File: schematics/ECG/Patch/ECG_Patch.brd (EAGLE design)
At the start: 11.6 x 27.7 mm, 10 parts

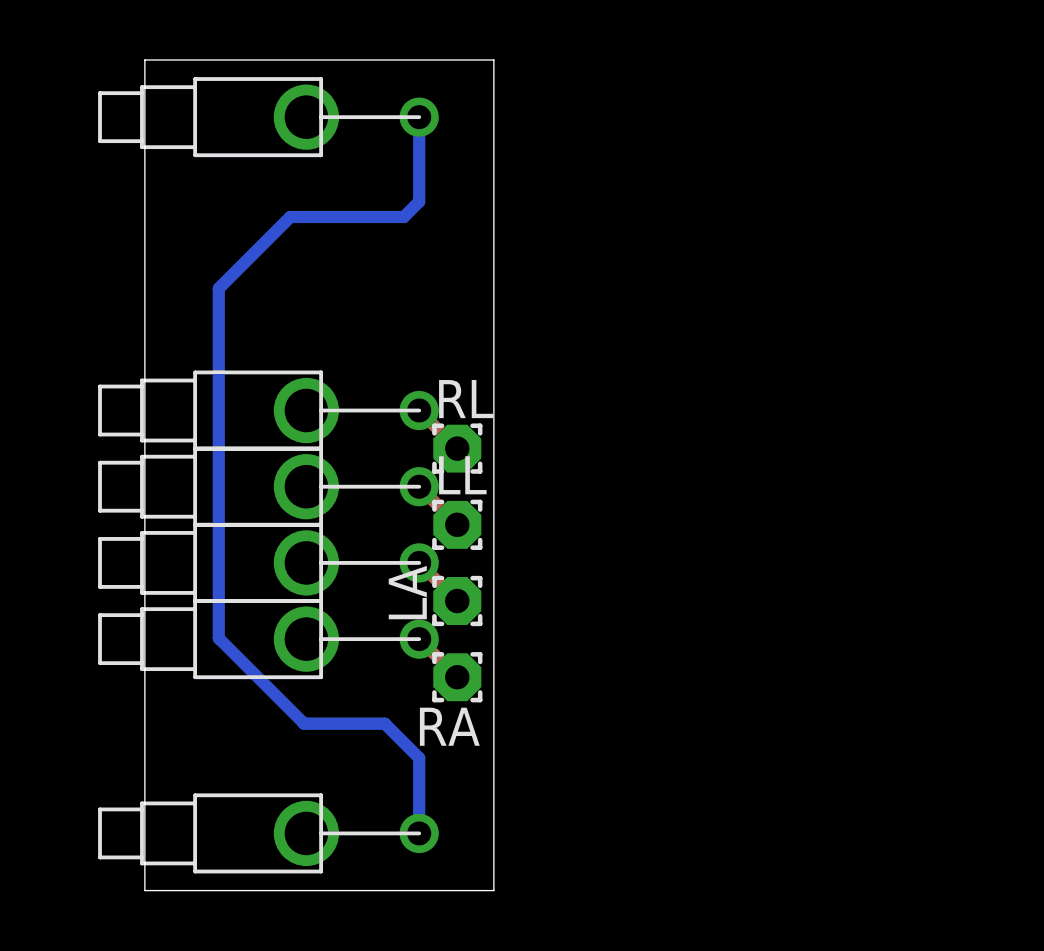
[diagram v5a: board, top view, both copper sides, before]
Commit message: tweaked traces
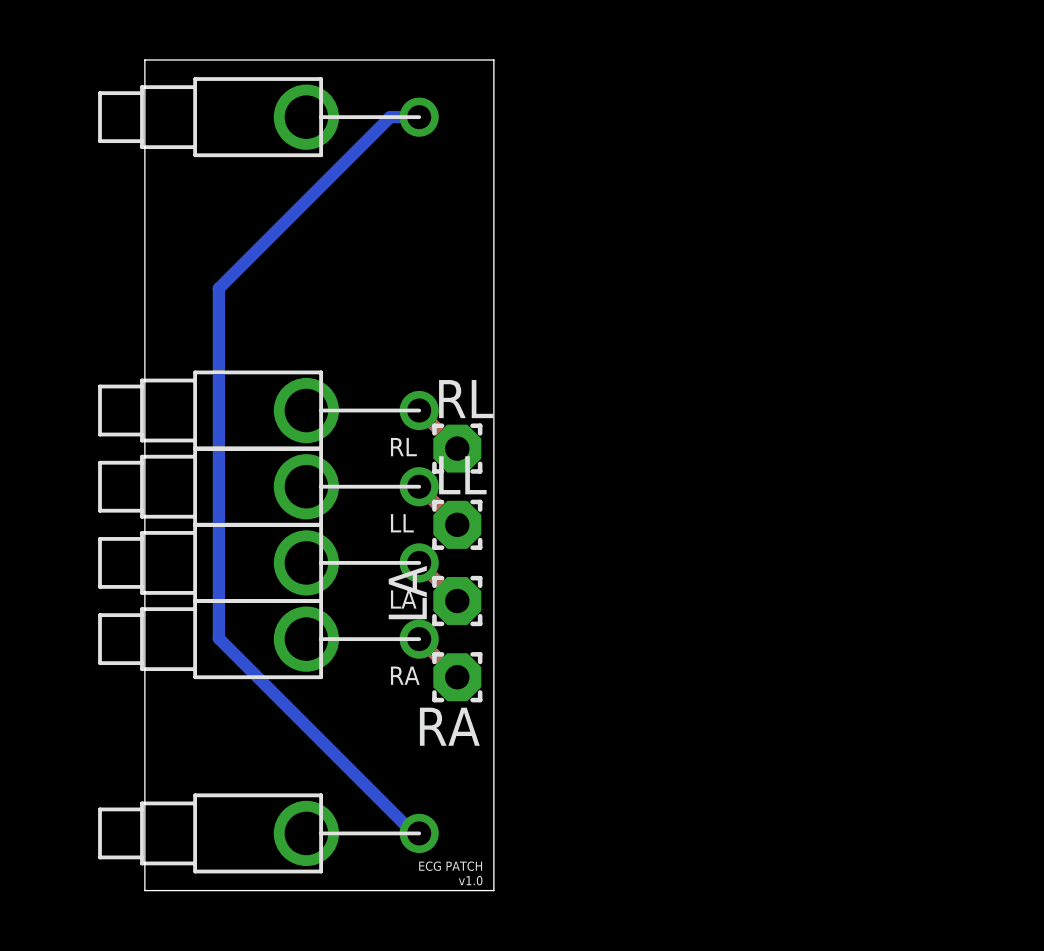
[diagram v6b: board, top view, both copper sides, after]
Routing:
- net BATT: track 33.2 -> 30.1 mm
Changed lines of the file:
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@@
 <wire x1="11.6332" y1="27.686" x2="0" y2="27.686" width="0" layer="20"/>
 <wire x1="0" y1="27.686" x2="0" y2="0" width="0" layer="20"/>
-<text x="8.128" y="14.478" size="0.6096" layer="48">RL</text>
-<text x="8.128" y="11.938" size="0.6096" layer="48">LL</text>
-<text x="8.128" y="9.398" size="0.6096" layer="48">LA</text>
-<text x="8.128" y="6.858" size="0.6096" layer="48">RA</text>
-<text x="11.2776" y="0.9652" size="0.3048" layer="48" rot="R180">ECG PATCH</text>
-<text x="11.2776" y="0.4826" size="0.3048" layer="48" rot="R180">v1.0</text>
+<text x="8.128" y="14.478" size="0.6096" layer="21">RL</text>
+<text x="8.128" y="11.938" size="0.6096" layer="21">LL</text>
+<text x="8.128" y="9.398" size="0.6096" layer="21">LA</text>
+<text x="8.128" y="6.858" size="0.6096" layer="21">RA</text>
+<text x="11.2776" y="0.9652" size="0.3048" layer="21" rot="R180">ECG PATCH</text>
+<text x="11.2776" y="0.4826" size="0.3048" layer="21" rot="R180">v1.0</text>
 </plain>
 <attributes>
@@
 <contactref element="U$6" pad="1"/>
 <wire x1="2.4638" y1="20.066" x2="2.4638" y2="8.4074" width="0.4064" layer="16"/>
-<wire x1="2.4638" y1="8.4074" x2="5.3086" y2="5.5626" width="0.4064" layer="16"/>
-<wire x1="9.144" y1="1.905" x2="9.144" y2="4.4196" width="0.4064" layer="16"/>
-<wire x1="9.144" y1="4.4196" x2="8.001" y2="5.5626" width="0.4064" layer="16"/>
-<wire x1="8.001" y1="5.5626" x2="5.3086" y2="5.5626" width="0.4064" layer="16"/>
-<wire x1="9.144" y1="25.781" x2="9.144" y2="22.9616" width="0.4064" layer="16"/>
-<wire x1="9.144" y1="22.9616" x2="8.636" y2="22.4536" width="0.4064" layer="16"/>
-<wire x1="8.636" y1="22.4536" x2="4.8514" y2="22.4536" width="0.4064" layer="16"/>
-<wire x1="4.8514" y1="22.4536" x2="2.4638" y2="20.066" width="0.4064" layer="16"/>
+<wire x1="9.144" y1="1.905" x2="8.9662" y2="1.905" width="0.4064" layer="16"/>
+<wire x1="8.9662" y1="1.905" x2="2.4638" y2="8.4074" width="0.4064" layer="16"/>
+<wire x1="9.144" y1="25.781" x2="8.1788" y2="25.781" width="0.4064" layer="16"/>
+<wire x1="8.1788" y1="25.781" x2="2.4638" y2="20.066" width="0.4064" layer="16"/>
 </signal>
 </signals>

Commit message: using updated millmax piston package with proper center origin
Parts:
- moved U$1 5.33 mm to (3.81, 16.0)
- moved U$2 5.33 mm to (3.81, 13.5)
- moved U$3 5.33 mm to (3.81, 10.9)
- moved U$4 5.33 mm to (3.81, 8.38)
- moved U$5 5.33 mm to (3.81, 25.8)
- moved U$6 5.33 mm to (3.81, 1.91)
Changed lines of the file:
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@@
 <?xml version="1.0" encoding="utf-8"?>
 <!DOCTYPE eagle SYSTEM "eagle.dtd">
-<eagle version="6.4">
+<eagle version="6.5.0">
 <drawing>
 <settings>
@@
 <layer number="220" name="220bmp" color="21" fill="1" visible="no" active="no"/>
 <layer number="221" name="221bmp" color="22" fill="1" visible="no" active="no"/>
-<layer number="222" name="222bmp" color="23" fill="1" visible="no" active="no"/>
 <layer number="223" name="223bmp" color="24" fill="1" visible="no" active="no"/>
 <layer number="224" name="224bmp" color="25" fill="1" visible="no" active="no"/>
@@
 </autorouter>
 <elements>
-<element name="U$1" library="pins" package="PISTON_RA_TH" value="PISTON_RA_TH" x="9.144" y="16.002" rot="R180"/>
-<element name="U$2" library="pins" package="PISTON_RA_TH" value="PISTON_RA_TH" x="9.144" y="13.462" rot="R180"/>
-<element name="U$3" library="pins" package="PISTON_RA_TH" value="PISTON_RA_TH" x="9.144" y="10.922" rot="R180"/>
-<element name="U$4" library="pins" package="PISTON_RA_TH" value="PISTON_RA_TH" x="9.144" y="8.382" rot="R180"/>
-<element name="U$5" library="pins" package="PISTON_RA_TH" value="PISTON_RA_TH" x="9.144" y="25.781" rot="R180"/>
-<element name="U$6" library="pins" package="PISTON_RA_TH" value="PISTON_RA_TH" x="9.144" y="1.905" rot="R180"/>
+<element name="U$1" library="pins" package="PISTON_RA_TH" value="PISTON_RA_TH" x="3.81" y="16.002" rot="R180"/>
+<element name="U$2" library="pins" package="PISTON_RA_TH" value="PISTON_RA_TH" x="3.81" y="13.462" rot="R180"/>
+<element name="U$3" library="pins" package="PISTON_RA_TH" value="PISTON_RA_TH" x="3.81" y="10.922" rot="R180"/>
+<element name="U$4" library="pins" package="PISTON_RA_TH" value="PISTON_RA_TH" x="3.81" y="8.382" rot="R180"/>
+<element name="U$5" library="pins" package="PISTON_RA_TH" value="PISTON_RA_TH" x="3.81" y="25.781" rot="R180"/>
+<element name="U$6" library="pins" package="PISTON_RA_TH" value="PISTON_RA_TH" x="3.81" y="1.905" rot="R180"/>
 <element name="LL" library="wirepad" package="1,6/0,8" value="" x="10.414" y="12.192"/>
 <element name="RL" library="wirepad" package="1,6/0,8" value="" x="10.414" y="14.732"/>

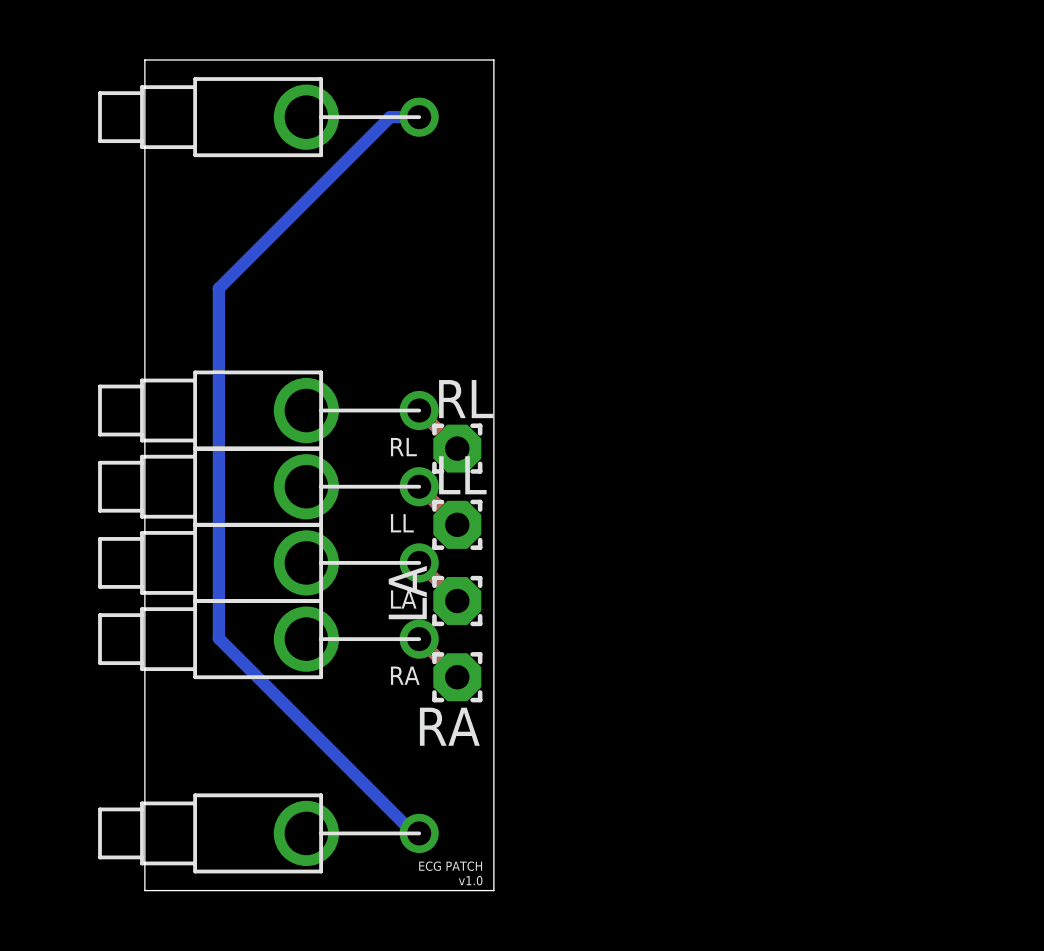
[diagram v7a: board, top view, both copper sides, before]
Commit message: using corrected piston package
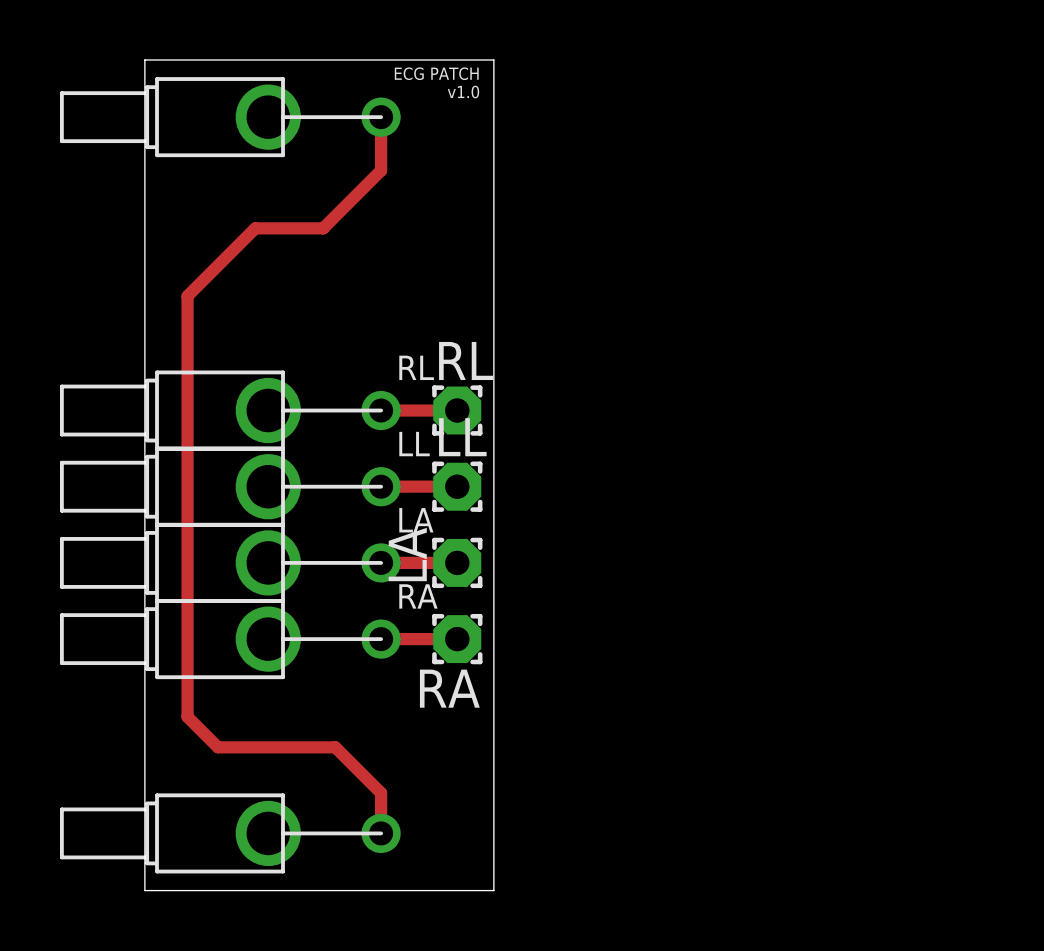
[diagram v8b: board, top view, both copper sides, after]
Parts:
- moved LA 1.27 mm to (10.4, 10.9)
- moved U$1 1.27 mm to (2.54, 16.0)
- moved U$2 1.27 mm to (2.54, 13.5)
- moved U$3 1.27 mm to (2.54, 10.9)
- moved U$4 1.27 mm to (2.54, 8.38)
- moved U$5 1.27 mm to (2.54, 25.8)
- moved U$6 1.27 mm to (2.54, 1.91)
- moved LL 1.27 mm to (10.4, 13.5)
- moved RA 1.27 mm to (10.4, 8.38)
- moved RL 1.27 mm to (10.4, 16.0)
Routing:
- net BATT: track 30.1 -> 32.8 mm
- net RL: track 1.80 -> 2.54 mm
- net RA: track 1.80 -> 2.54 mm
- net LL: track 1.80 -> 2.54 mm
- net LA: track 1.80 -> 2.54 mm
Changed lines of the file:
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@@
 <?xml version="1.0" encoding="utf-8"?>
 <!DOCTYPE eagle SYSTEM "eagle.dtd">
-<eagle version="6.5.0">
+<eagle version="6.4">
 <drawing>
 <settings>
@@
 <wire x1="11.6332" y1="27.686" x2="0" y2="27.686" width="0" layer="20"/>
 <wire x1="0" y1="27.686" x2="0" y2="0" width="0" layer="20"/>
-<text x="8.128" y="14.478" size="0.6096" layer="21">RL</text>
-<text x="8.128" y="11.938" size="0.6096" layer="21">LL</text>
-<text x="8.128" y="9.398" size="0.6096" layer="21">LA</text>
-<text x="8.128" y="6.858" size="0.6096" layer="21">RA</text>
-<text x="11.2776" y="0.9652" size="0.3048" layer="21" rot="R180">ECG PATCH</text>
-<text x="11.2776" y="0.4826" size="0.3048" layer="21" rot="R180">v1.0</text>
+<text x="8.382" y="17.018" size="0.8128" layer="21">RL</text>
+<text x="8.382" y="14.478" size="0.8128" layer="21">LL</text>
+<text x="8.382" y="11.938" size="0.8128" layer="21">LA</text>
+<text x="8.382" y="9.398" size="0.8128" layer="21">RA</text>
+<text x="11.176" y="27.432" size="0.4064" layer="21" rot="R180">ECG PATCH</text>
+<text x="11.176" y="26.8224" size="0.4064" layer="21" rot="R180">v1.0</text>
 </plain>
 <attributes>
@@
 </autorouter>
 <elements>
-<element name="U$1" library="pins" package="PISTON_RA_TH" value="PISTON_RA_TH" x="3.81" y="16.002" rot="R180"/>
-<element name="U$2" library="pins" package="PISTON_RA_TH" value="PISTON_RA_TH" x="3.81" y="13.462" rot="R180"/>
-<element name="U$3" library="pins" package="PISTON_RA_TH" value="PISTON_RA_TH" x="3.81" y="10.922" rot="R180"/>
-<element name="U$4" library="pins" package="PISTON_RA_TH" value="PISTON_RA_TH" x="3.81" y="8.382" rot="R180"/>
-<element name="U$5" library="pins" package="PISTON_RA_TH" value="PISTON_RA_TH" x="3.81" y="25.781" rot="R180"/>
-<element name="U$6" library="pins" package="PISTON_RA_TH" value="PISTON_RA_TH" x="3.81" y="1.905" rot="R180"/>
-<element name="LL" library="wirepad" package="1,6/0,8" value="" x="10.414" y="12.192"/>
-<element name="RL" library="wirepad" package="1,6/0,8" value="" x="10.414" y="14.732"/>
-<element name="LA" library="wirepad" package="1,6/0,8" value="" x="10.414" y="9.652" rot="R90"/>
-<element name="RA" library="wirepad" package="1,6/0,8" value="" x="10.414" y="7.112" rot="R180"/>
+<element name="U$1" library="pins" package="PISTON_RA_TH" value="PISTON_RA_TH" x="2.54" y="16.002" rot="R180"/>
+<element name="U$2" library="pins" package="PISTON_RA_TH" value="PISTON_RA_TH" x="2.54" y="13.462" rot="R180"/>
+<element name="U$3" library="pins" package="PISTON_RA_TH" value="PISTON_RA_TH" x="2.54" y="10.922" rot="R180"/>
+<element name="U$4" library="pins" package="PISTON_RA_TH" value="PISTON_RA_TH" x="2.54" y="8.382" rot="R180"/>
+<element name="U$5" library="pins" package="PISTON_RA_TH" value="PISTON_RA_TH" x="2.54" y="25.781" rot="R180"/>
+<element name="U$6" library="pins" package="PISTON_RA_TH" value="PISTON_RA_TH" x="2.54" y="1.905" rot="R180"/>
+<element name="LL" library="wirepad" package="1,6/0,8" value="" x="10.414" y="13.462"/>
+<element name="RL" library="wirepad" package="1,6/0,8" value="" x="10.414" y="16.002"/>
+<element name="LA" library="wirepad" package="1,6/0,8" value="" x="10.414" y="10.922" rot="R90"/>
+<element name="RA" library="wirepad" package="1,6/0,8" value="" x="10.414" y="8.382" rot="R180"/>
 </elements>
 <signals>
@@
 <contactref element="U$2" pad="1"/>
 <contactref element="LL" pad="1"/>
-<wire x1="10.414" y1="12.192" x2="9.144" y2="13.462" width="0.4064" layer="1"/>
+<wire x1="7.874" y1="13.462" x2="10.414" y2="13.462" width="0.4064" layer="1"/>
 </signal>
 <signal name="RL">
 <contactref element="U$1" pad="1"/>
 <contactref element="RL" pad="1"/>
-<wire x1="10.414" y1="14.732" x2="9.144" y2="16.002" width="0.4064" layer="1"/>
+<wire x1="7.874" y1="16.002" x2="10.414" y2="16.002" width="0.4064" layer="1"/>
 </signal>
 <signal name="LA">
 <contactref element="U$3" pad="1"/>
 <contactref element="LA" pad="1"/>
-<wire x1="10.414" y1="9.652" x2="9.144" y2="10.922" width="0.4064" layer="1"/>
+<wire x1="7.874" y1="10.922" x2="10.414" y2="10.922" width="0.4064" layer="1"/>
 </signal>
 <signal name="RA">
 <contactref element="U$4" pad="1"/>
 <contactref element="RA" pad="1"/>
-<wire x1="10.414" y1="7.112" x2="9.144" y2="8.382" width="0.4064" layer="1"/>
+<wire x1="7.874" y1="8.382" x2="10.414" y2="8.382" width="0.4064" layer="1"/>
 </signal>
 <signal name="BATT">
 <contactref element="U$5" pad="1"/>
 <contactref element="U$6" pad="1"/>
-<wire x1="2.4638" y1="20.066" x2="2.4638" y2="8.4074" width="0.4064" layer="16"/>
-<wire x1="9.144" y1="1.905" x2="8.9662" y2="1.905" width="0.4064" layer="16"/>
-<wire x1="8.9662" y1="1.905" x2="2.4638" y2="8.4074" width="0.4064" layer="16"/>
-<wire x1="9.144" y1="25.781" x2="8.1788" y2="25.781" width="0.4064" layer="16"/>
-<wire x1="8.1788" y1="25.781" x2="2.4638" y2="20.066" width="0.4064" layer="16"/>
+<wire x1="1.4224" y1="5.7912" x2="1.4224" y2="19.812" width="0.4064" layer="1"/>
+<wire x1="7.874" y1="1.905" x2="7.874" y2="3.2512" width="0.4064" layer="1"/>
+<wire x1="1.4224" y1="5.7912" x2="2.4384" y2="4.7752" width="0.4064" layer="1"/>
+<wire x1="2.4384" y1="4.7752" x2="6.35" y2="4.7752" width="0.4064" layer="1"/>
+<wire x1="6.35" y1="4.7752" x2="7.874" y2="3.2512" width="0.4064" layer="1"/>
+<wire x1="1.4224" y1="19.812" x2="3.683" y2="22.0726" width="0.4064" layer="1"/>
+<wire x1="3.683" y1="22.0726" x2="5.9436" y2="22.0726" width="0.4064" layer="1"/>
+<wire x1="5.9436" y1="22.0726" x2="7.874" y2="24.003" width="0.4064" layer="1"/>
+<wire x1="7.874" y1="24.003" x2="7.874" y2="25.781" width="0.4064" layer="1"/>
 </signal>
 </signals>
